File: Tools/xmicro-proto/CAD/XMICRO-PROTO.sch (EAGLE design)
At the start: 1 part

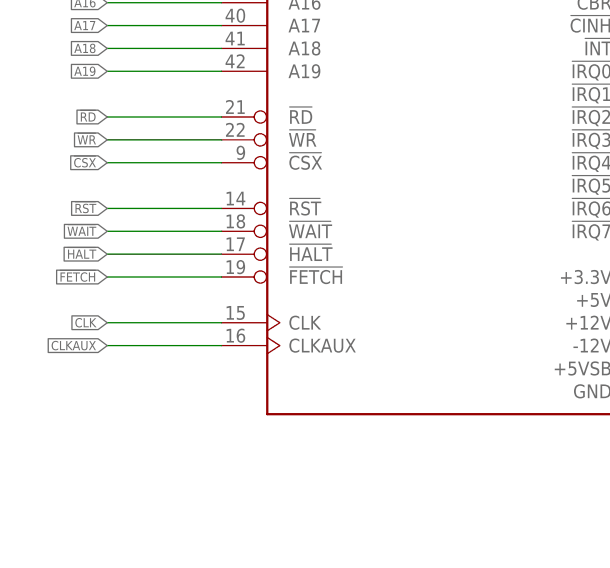
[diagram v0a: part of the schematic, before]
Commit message: Fixed tools with new IOSEL signal
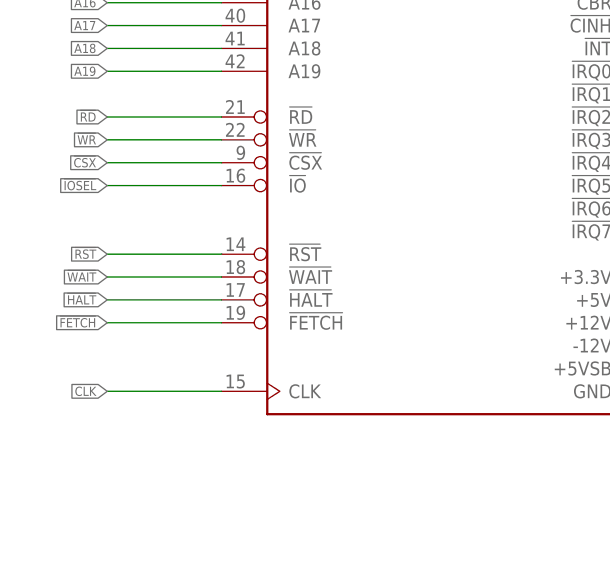
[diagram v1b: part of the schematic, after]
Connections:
- removed net CLKAUX: PC0.CLKAUX@16
- new net !IOSEL: PC0.!IO@16
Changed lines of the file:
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@@
 <segment>
 <pinref part="PC0" gate="G$1" pin="!RST@14"/>
-<wire x1="111.76" y1="78.74" x2="99.06" y2="78.74" width="0.1524" layer="91"/>
-<label x="99.06" y="78.74" size="1.016" layer="95" rot="R180" xref="yes"/>
+<wire x1="111.76" y1="73.66" x2="99.06" y2="73.66" width="0.1524" layer="91"/>
+<label x="99.06" y="73.66" size="1.016" layer="95" rot="R180" xref="yes"/>
 </segment>
 </net>
@@
 <segment>
 <pinref part="PC0" gate="G$1" pin="!WAIT@18"/>
-<wire x1="111.76" y1="76.2" x2="99.06" y2="76.2" width="0.1524" layer="91"/>
-<label x="99.06" y="76.2" size="1.016" layer="95" rot="R180" xref="yes"/>
+<wire x1="111.76" y1="71.12" x2="99.06" y2="71.12" width="0.1524" layer="91"/>
+<label x="99.06" y="71.12" size="1.016" layer="95" rot="R180" xref="yes"/>
 </segment>
 </net>
@@
 <segment>
 <pinref part="PC0" gate="G$1" pin="!HALT@17"/>
-<wire x1="111.76" y1="73.66" x2="99.06" y2="73.66" width="0.1524" layer="91"/>
-<label x="99.06" y="73.66" size="1.016" layer="95" rot="R180" xref="yes"/>
+<wire x1="111.76" y1="68.58" x2="99.06" y2="68.58" width="0.1524" layer="91"/>
+<label x="99.06" y="68.58" size="1.016" layer="95" rot="R180" xref="yes"/>
 </segment>
 </net>
@@
 <segment>
 <pinref part="PC0" gate="G$1" pin="!FETCH@19"/>
-<wire x1="111.76" y1="71.12" x2="99.06" y2="71.12" width="0.1524" layer="91"/>
-<label x="99.06" y="71.12" size="1.016" layer="95" rot="R180" xref="yes"/>
+<wire x1="111.76" y1="66.04" x2="99.06" y2="66.04" width="0.1524" layer="91"/>
+<label x="99.06" y="66.04" size="1.016" layer="95" rot="R180" xref="yes"/>
 </segment>
 </net>
@@
 <segment>
 <pinref part="PC0" gate="G$1" pin="CLK@15"/>
-<wire x1="111.76" y1="66.04" x2="99.06" y2="66.04" width="0.1524" layer="91"/>
-<label x="99.06" y="66.04" size="1.016" layer="95" rot="R180" xref="yes"/>
+<wire x1="111.76" y1="58.42" x2="99.06" y2="58.42" width="0.1524" layer="91"/>
+<label x="99.06" y="58.42" size="1.016" layer="95" rot="R180" xref="yes"/>
 </segment>
 </net>
-<net name="CLKAUX" class="0">
+<net name="!IOSEL" class="0">
 <segment>
-<pinref part="PC0" gate="G$1" pin="CLKAUX@16"/>
-<wire x1="111.76" y1="63.5" x2="99.06" y2="63.5" width="0.1524" layer="91"/>
-<label x="99.06" y="63.5" size="1.016" layer="95" rot="R180" xref="yes"/>
+<pinref part="PC0" gate="G$1" pin="!IO@16"/>
+<label x="99.06" y="81.28" size="1.016" layer="95" rot="R180" xref="yes"/>
+<wire x1="111.76" y1="81.28" x2="99.06" y2="81.28" width="0.1524" layer="91"/>
 </segment>
 </net>
